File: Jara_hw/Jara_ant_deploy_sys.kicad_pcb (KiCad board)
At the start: 2 copper layers, 80 x 80 mm, 16 parts, among them J2 Conn_01x15, J3 Conn_01x10, Q1 Q_NMOS_GSD, Q2 Q_NMOS_GSD, SW3 SW_SPDT_312, SW4 SW_SPDT_312, U2 RFM95W-868S2

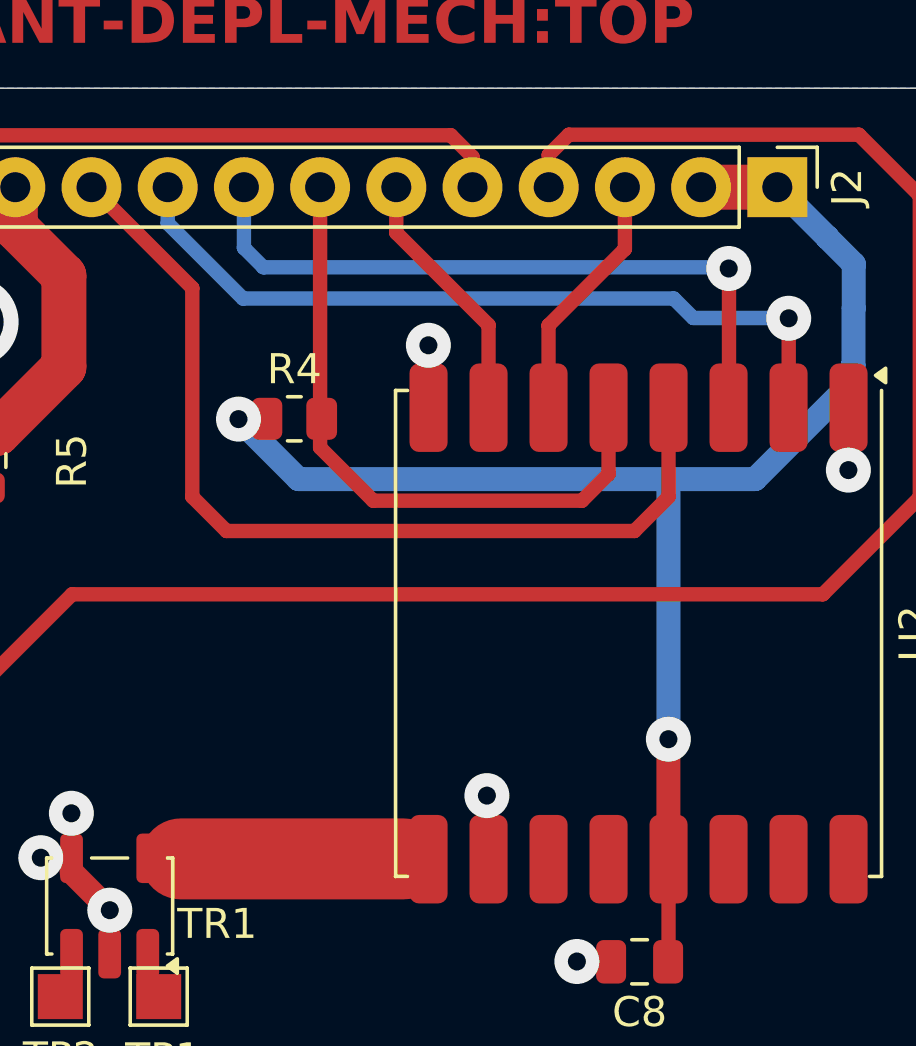
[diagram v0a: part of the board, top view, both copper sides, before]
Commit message: DIO7 changed to DIO0 on Jára PCB to be compatibile with the LoRa Arduino library
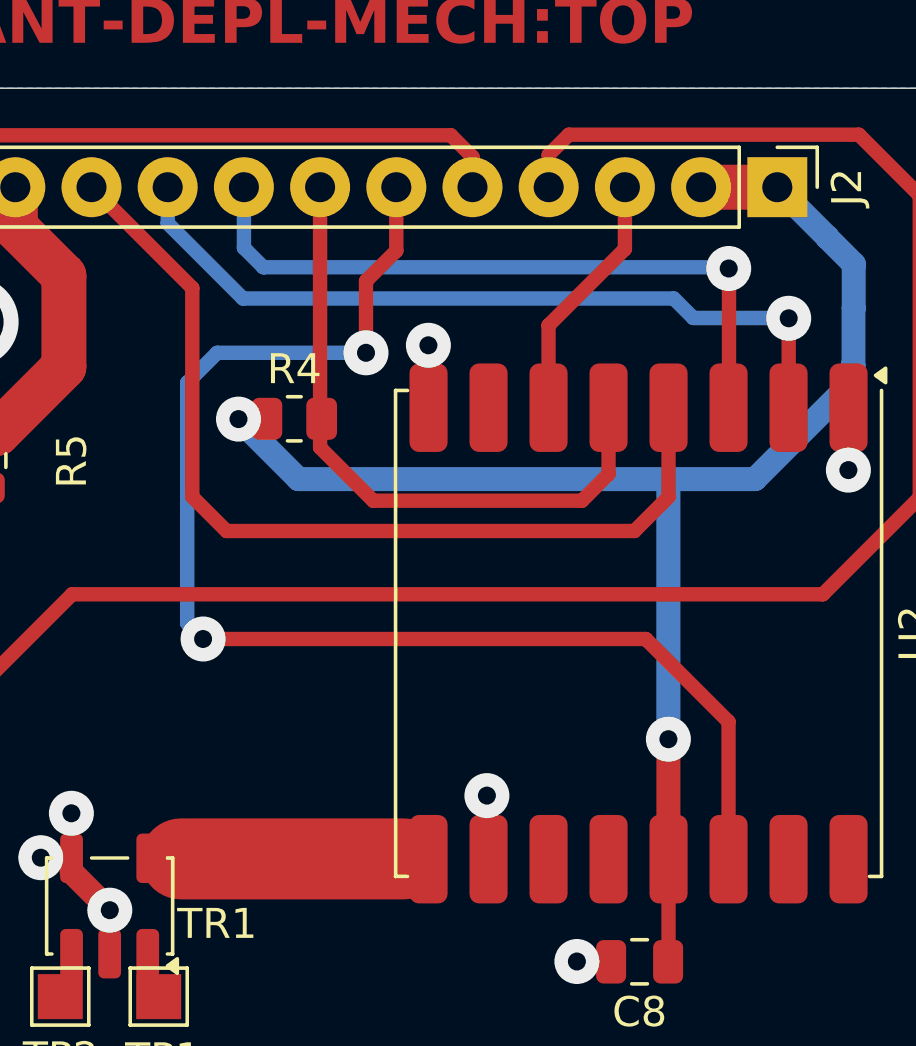
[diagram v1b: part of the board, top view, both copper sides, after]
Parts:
- TP1, TP2: value TestPoint -> (none)
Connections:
- J2 pad 6: /DIO7 -> /DIO0
- TR1 pad 2: GND -> (no net)
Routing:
- net /DIO0: track 0.00 -> 44.3 mm, vias 0 -> 2
- net /DIO7: track 8.63 -> 0.01 mm
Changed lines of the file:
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@@
 		)
 		(property ki_fp_filters "Transformer*AT224*")
-		(sheetname "Hlavní")
-		(sheetfile "ant_deployment_electronics.kicad_sch")
+		(sheetname "Root")
+		(sheetfile "Jara_ant_deploy_sys.kicad_sch")
 		(attr smd)
 		(fp_line
@@
 			(layers "F.Cu" "F.Paste" "F.Mask")
 			(roundrect_rratio 0.25)
-			(net 1 "GND")
 		)
 		(pad "3" smd roundrect
@@
 			)
 		)
-		(sheetname "Hlavní")
-		(sheetfile "ant_deployment_electronics.kicad_sch")
+		(sheetname "Root")
+		(sheetfile "Jara_ant_deploy_sys.kicad_sch")
 		(attr through_hole)
 		(fp_line
@@
 		)
 		(property ki_fp_filters "Connector*:*_1x??_*")
-		(sheetname "Hlavní")
-		(sheetfile "ant_deployment_electronics.kicad_sch")
+		(sheetname "Root")
+		(sheetfile "Jara_ant_deploy_sys.kicad_sch")
 		(attr through_hole)
 		(fp_line
@@
 		)
 		(property ki_fp_filters "C_*")
-		(sheetname "Hlavní")
-		(sheetfile "ant_deployment_electronics.kicad_sch")
+		(sheetname "Root")
+		(sheetfile "Jara_ant_deploy_sys.kicad_sch")
 		(attr smd)
 		(fp_line
@@
 		)
 		(property ki_fp_filters "R_*")
-		(sheetname "Hlavní")
-		(sheetfile "ant_deployment_electronics.kicad_sch")
+		(sheetname "Root")
+		(sheetfile "Jara_ant_deploy_sys.kicad_sch")
 		(attr smd)
 		(fp_line
@@
 			)
 		)
-		(property "Value" "TestPoint"
+		(property "Value" " "
 			(at 0 1.75 -90)
 			(layer "F.Fab")
@@
 		)
 		(property ki_fp_filters "Pin* Test*")
-		(sheetname "Hlavní")
-		(sheetfile "ant_deployment_electronics.kicad_sch")
+		(sheetname "Root")
+		(sheetfile "Jara_ant_deploy_sys.kicad_sch")
 		(attr exclude_from_pos_files)
 		(fp_line
@@
 		)
 		(property ki_fp_filters "R_*")
-		(sheetname "Hlavní")
-		(sheetfile "ant_deployment_electronics.kicad_sch")
+		(sheetname "Root")
+		(sheetfile "Jara_ant_deploy_sys.kicad_sch")
 		(attr smd)
 		(fp_line
@@
 		)
 		(property ki_fp_filters "Connector*:*_1x??_*")
-		(sheetname "Hlavní")
-		(sheetfile "ant_deployment_electronics.kicad_sch")
+		(sheetname "Root")
+		(sheetfile "Jara_ant_deploy_sys.kicad_sch")
 		(attr through_hole)
 		(fp_line
@@
 			(layers "*.Cu" "*.Mask")
 			(remove_unused_layers no)
-			(net 7 "/DIO7")
+			(net 13 "/DIO0")
 			(pinfunction "Pin_6")
 			(pintype "passive")
@@
 			)
 		)
-		(sheetname "Hlavní")
-		(sheetfile "ant_deployment_electronics.kicad_sch")
+		(sheetname "Root")
+		(sheetfile "Jara_ant_deploy_sys.kicad_sch")
 		(attr through_hole)
 		(fp_line
@@
 			)
 		)
-		(sheetname "Hlavní")
-		(sheetfile "ant_deployment_electronics.kicad_sch")
+		(sheetname "Root")
+		(sheetfile "Jara_ant_deploy_sys.kicad_sch")
 		(attr smd)
 		(fp_line
@@
 		)
 		(property ki_fp_filters "HOPERF*RFM9XW*")
-		(sheetname "Hlavní")
-		(sheetfile "ant_deployment_electronics.kicad_sch")
+		(sheetname "Root")
+		(sheetfile "Jara_ant_deploy_sys.kicad_sch")
 		(attr smd)
 		(fp_line
@@
 		)
 		(property ki_fp_filters "R_*")
-		(sheetname "Hlavní")
-		(sheetfile "ant_deployment_electronics.kicad_sch")
+		(sheetname "Root")
+		(sheetfile "Jara_ant_deploy_sys.kicad_sch")
 		(attr smd)
 		(fp_line
@@
 		)
 		(property ki_fp_filters "R_*")
-		(sheetname "Hlavní")
-		(sheetfile "ant_deployment_electronics.kicad_sch")
+		(sheetname "Root")
+		(sheetfile "Jara_ant_deploy_sys.kicad_sch")
 		(attr smd)
 		(fp_line
@@
 			)
 		)
-		(sheetname "Hlavní")
-		(sheetfile "ant_deployment_electronics.kicad_sch")
+		(sheetname "Root")
+		(sheetfile "Jara_ant_deploy_sys.kicad_sch")
 		(attr smd)
 		(fp_line
@@
 		)
 		(property ki_fp_filters "R_*")
-		(sheetname "Hlavní")
-		(sheetfile "ant_deployment_electronics.kicad_sch")
+		(sheetname "Root")
+		(sheetfile "Jara_ant_deploy_sys.kicad_sch")
 		(attr smd)
 		(fp_line
@@
 			)
 		)
-		(property "Value" "TestPoint"
+		(property "Value" " "
 			(at 0.63 -2.86 -90)
 			(layer "F.Fab")
@@
 		)
 		(property ki_fp_filters "Pin* Test*")
-		(sheetname "Hlavní")
-		(sheetfile "ant_deployment_electronics.kicad_sch")
+		(sheetname "Root")
+		(sheetfile "Jara_ant_deploy_sys.kicad_sch")
 		(attr exclude_from_pos_files)
 		(fp_line
@@
 	)
 	(segment
-		(start 171.475 62.895)
-		(end 171.475 65.65)
-		(width 0.48)
-		(layer "F.Cu")
-		(net 7)
-	)
-	(segment
-		(start 168.4 59.82)
-		(end 171.475 62.895)
-		(width 0.48)
-		(layer "F.Cu")
-		(net 7)
-	)
-	(segment
-		(start 168.4 58.3)
-		(end 168.4 59.82)
-		(width 0.48)
-		(layer "F.Cu")
-		(net 7)
-	)
-	(segment
 		(start 179.49 65.635)
 		(end 179.475 65.65)
@@
 	)
 	(segment
+		(start 179.475 76.118087)
+		(end 176.716913 73.36)
+		(width 0.48)
+		(layer "F.Cu")
+		(net 13)
+	)
+	(segment
+		(start 168.4 60.42)
+		(end 168.4 58.3)
+		(width 0.48)
+		(layer "F.Cu")
+		(net 13)
+	)
+	(segment
+		(start 167.39 61.43)
+		(end 168.4 60.42)
+		(width 0.48)
+		(layer "F.Cu")
+		(net 13)
+	)
+	(segment
+		(start 176.716913 73.36)
+		(end 161.96 73.36)
+		(width 0.48)
+		(layer "F.Cu")
+		(net 13)
+	)
+	(segment
+		(start 179.475 80.7)
+		(end 179.475 76.118087)
+		(width 0.48)
+		(layer "F.Cu")
+		(net 13)
+	)
+	(segment
+		(start 167.39 63.82)
+		(end 167.39 61.43)
+		(width 0.48)
+		(layer "F.Cu")
+		(net 13)
+	)
+	(via
+		(at 161.96 73.36)
+		(size 1.5)
+		(drill 0.6)
+		(layers "F.Cu" "B.Cu")
+		(net 13)
+	)
+	(via
+		(at 167.39 63.82)
+		(size 1.5)
+		(drill 0.6)
+		(layers "F.Cu" "B.Cu")
+		(net 13)
+	)
+	(segment
+		(start 161.43 72.83)
+		(end 161.43 64.82)
+		(width 0.48)
+		(layer "B.Cu")
+		(net 13)
+	)
+	(segment
+		(start 162.43 63.82)
+		(end 167.39 63.82)
+		(width 0.48)
+		(layer "B.Cu")
+		(net 13)
+	)
+	(segment
+		(start 161.43 64.82)
+		(end 162.43 63.82)
+		(width 0.48)
+		(layer "B.Cu")
+		(net 13)
+	)
+	(segment
+		(start 161.96 73.36)
+		(end 161.43 72.83)
+		(width 0.48)
+		(layer "B.Cu")
+		(net 13)
+	)
+	(segment
